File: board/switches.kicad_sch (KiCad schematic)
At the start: 21 parts, among them J2 SS-73100-082, Q2 IPB180N10S4-02, Q5 IPB180N10S4-02, Q6 IPB180N10S4-02, Q7 IPB180N10S4-02, Q8 IPB180N10S4-02, U1 LT1910, U11 LT1910, U12 LT1910, U13 LT1910, U14 LT1910

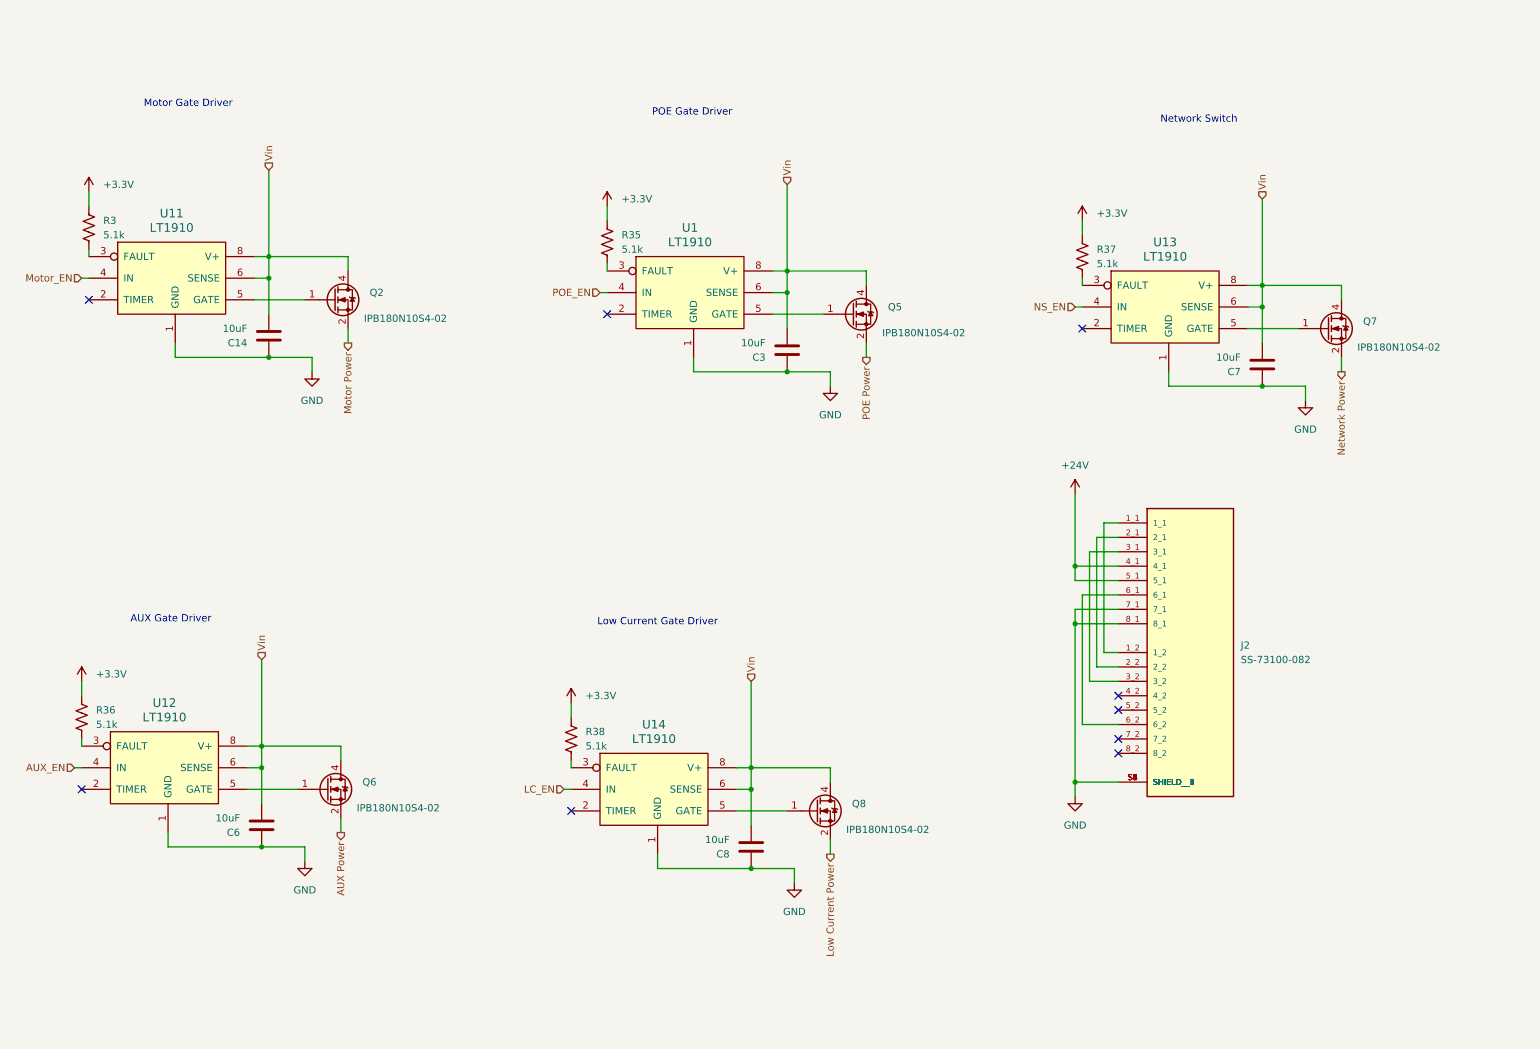
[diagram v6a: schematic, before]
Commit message: add 2 new POE and replace mosfets
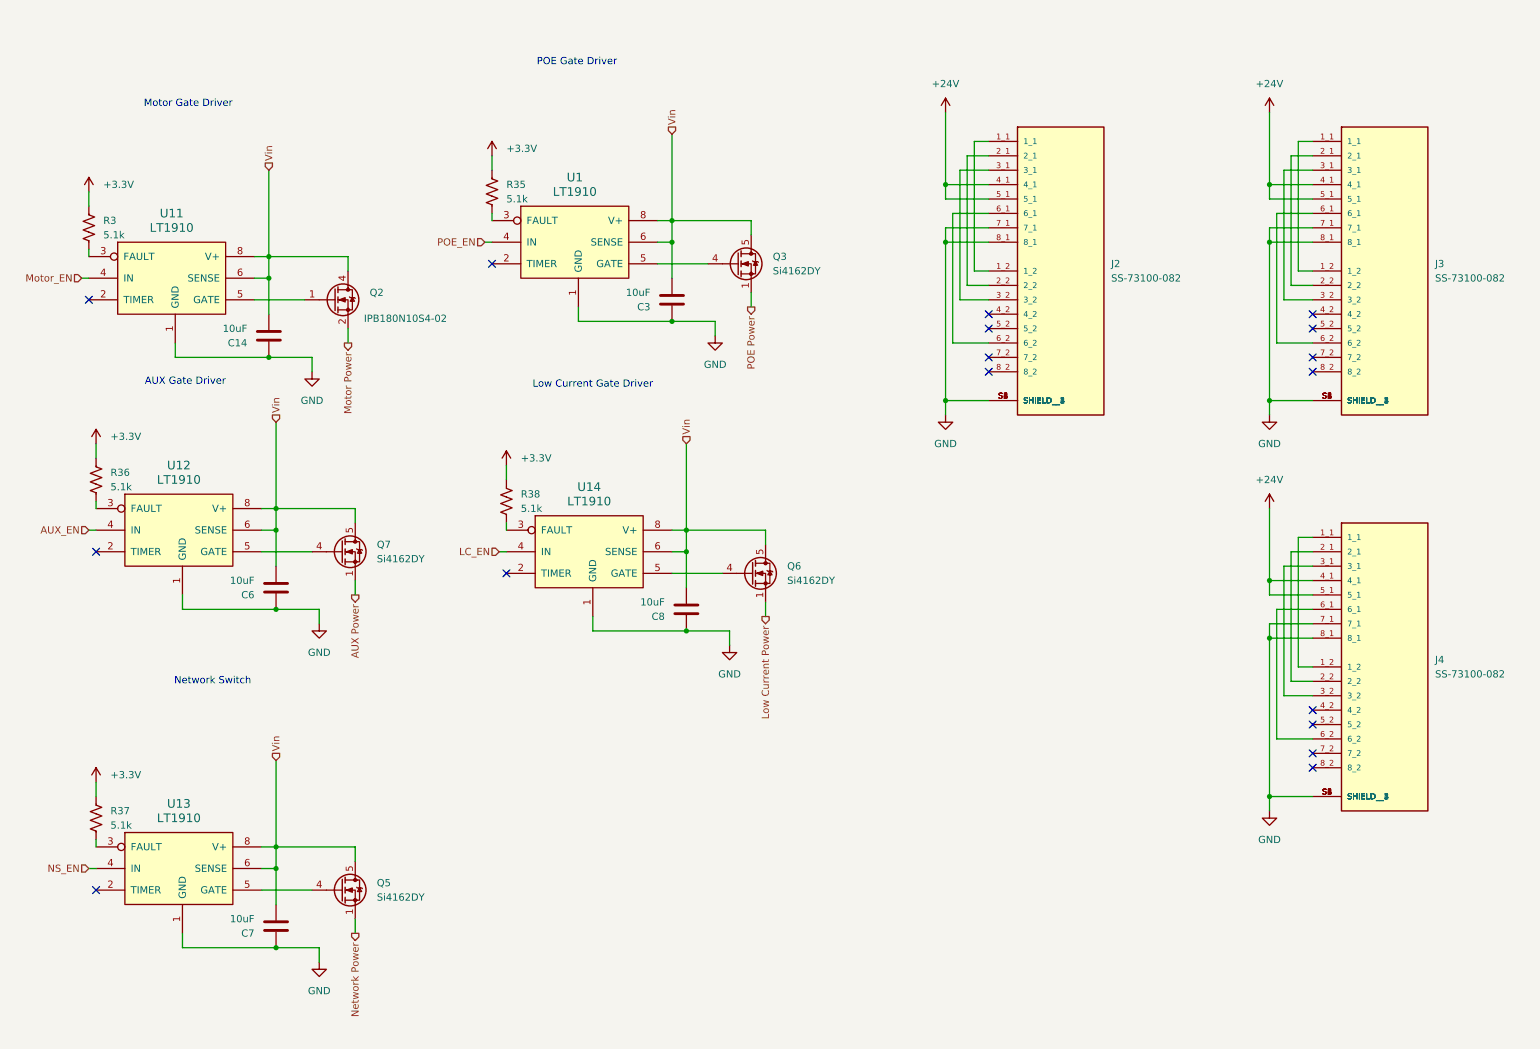
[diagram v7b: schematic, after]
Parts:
- removed Q5, Q6, Q7, Q8: IPB180N10S4-02, Package_TO_SOT_SMD:TO-263-6, symbol Transistor_FET:IPB180N10S4-02
- added J3, J4: SS-73100-082, SS-73100-082:BEL_SS-73100-082, symbol PowerManagementBoard:SS-73100-082
- added Q3, Q5, Q6, Q7: Si4162DY, Package_SO:SOIC-8_3.9x4.9mm_P1.27mm, symbol Transistor_FET:Si4162DY
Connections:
- net +24V: now also J3.4_1, J3.5_1, J4.4_1, J4.5_1
- net AUX Power: now also Q7.1 (S), Q7.2 (S), Q7.3 (S)
- net GND: now also J3.7_1, J3.8_1, J3.S1 (SHIELD), J3.S2 (SHIELD__1), J3.S3 (SHIELD__2), J3.S4 (SHIELD__3), J3.S5 (SHIELD__4), J3.S6 (SHIELD__5), J4.7_1, J4.8_1, J4.S1 (SHIELD), J4.S2 (SHIELD__1), J4.S3 (SHIELD__2), J4.S4 (SHIELD__3), J4.S5 (SHIELD__4), J4.S6 (SHIELD__5)
- net Low Current Power: now also Q6.1 (S), Q6.2 (S), Q6.3 (S)
- net Network Power: now also Q5.1 (S), Q5.2 (S), Q5.3 (S)
- net POE Power: now also Q3.1 (S), Q3.2 (S), Q3.3 (S)
- net Vin: now also Q3.5 (D), Q3.6 (D), Q3.7 (D), Q3.8 (D), Q5.5 (D), Q5.6 (D), Q5.7 (D), Q5.8 (D), Q6.5 (D), Q6.6 (D), Q6.7 (D), Q6.8 (D), Q7.5 (D), Q7.6 (D), Q7.7 (D), Q7.8 (D)
- net at U13.5 (GATE): now also Q5.4 (G)
- net at U14.5 (GATE): now also Q6.4 (G)
- net at U12.5 (GATE): now also Q7.4 (G)
- net at U1.5 (GATE): now also Q3.4 (G)
- new net: J4.1_1, J4.1_2
- new net: J4.2_1, J4.2_2
- new net: J4.3_1, J4.3_2
- new net: J4.6_1, J4.6_2
- new net: J3.1_1, J3.1_2
- new net: J3.2_1, J3.2_2
- new net: J3.3_1, J3.3_2
- new net: J3.6_1, J3.6_2
- no-connect marks 9 -> 17
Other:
- moved on the sheet: C3, C6, C7, C8, J2, R35, R36, R37, R38, U1, U12, U13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

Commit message: Current Sensors FABRICATED
Current Sensor Hierarchy sheet created
Contains:
- Network Switch current sensing
- POE current sensing
- Low Current current sensing
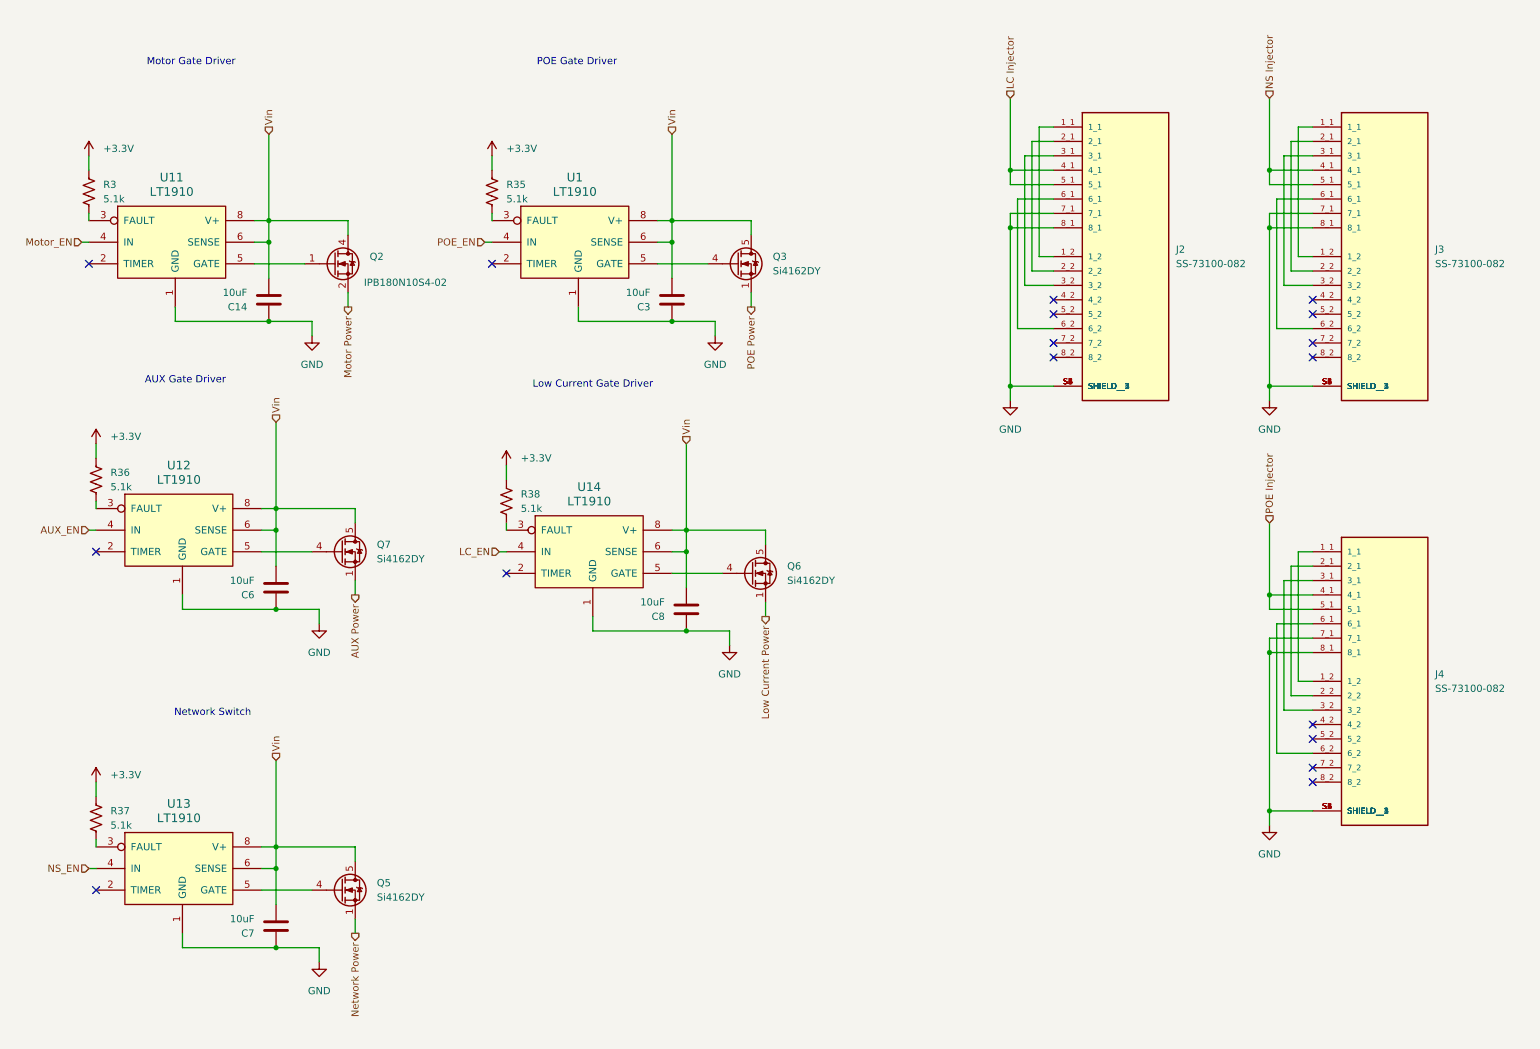
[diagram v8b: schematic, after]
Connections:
- removed net +24V: J2.4_1, J2.5_1, J3.4_1, J3.5_1, J4.4_1, J4.5_1
- new net LC Injector: J2.4_1, J2.5_1
- new net NS Injector: J3.4_1, J3.5_1
- new net POE Injector: J4.4_1, J4.5_1
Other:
- moved on the sheet: C14, J2, J3, J4, Q2, R3, U11
